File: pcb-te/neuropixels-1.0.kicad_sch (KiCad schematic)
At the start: 15 parts, among them J2 1-2013496-8, U6 MAX40111ANT

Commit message: Added new fields (OEPS PN, MPN, and Type) to all components.
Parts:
- C28, C29: MPN (none) -> GRM033R61E104KE14J; OEPS PN (none) -> OEPS010035; Type (none) -> SMD
- C30: MPN (none) -> GRM033R71E103KE14D; OEPS PN (none) -> OEPS010037; Type (none) -> SMD
- C31: MPN (none) -> GRM0335C1H270GA01D; OEPS PN (none) -> OEPS010029; Type (none) -> SMD
- J2: MPN (none) -> 1-2013496-8; OEPS PN (none) -> OEPS070051; Type (none) -> SMD
- R? (x3): MPN (none) -> RC0201FR-071KL; OEPS PN (none) -> OEPS020065; Type (none) -> SMD
- R?: MPN (none) -> RMCF0201FT22R0CT-ND; OEPS PN (none) -> OEPS020069; Type (none) -> SMD
- R?: MPN (none) -> CRCW02017K15FKED; OEPS PN (none) -> OEPS020058; Type (none) -> SMD
- R?: MPN (none) -> CRCW020110K0FNED; OEPS PN (none) -> OEPS020066; Type (none) -> SMD
- R?: MPN (none) -> RC0201FR-0749R9L; OEPS PN (none) -> OEPS020068; Type (none) -> SMD
- U6: MPN (none) -> MAX40111ANT+; OEPS PN (none) -> OEPS080048; Type (none) -> SMD
- U?: MPN (none) -> DSC6101MA3B-PROGT; OEPS PN (none) -> OEPS080049; Type (none) -> SMD
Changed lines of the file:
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@@
+      (effects (font (size 1.27 1.27)) hide)
+    )
+    (property "MPN" "GRM033R61E104KE14J" (at 59.69 72.39 0)
+      (effects (font (size 1.27 1.27)) hide)
+    )
+    (property "OEPS PN" "OEPS010035" (at 59.69 72.39 0)
+      (effects (font (size 1.27 1.27)) hide)
+    )
+    (property "Type" "SMD" (at 59.69 72.39 0)
+      (effects (font (size 1.27 1.27)) hide)
+    )
+    (property "test" "" (at 59.69 72.39 0)
       (effects (font (size 1.27 1.27)) hide)
     )
@@
     )
     (property "Datasheet" "https://www.analog.com/media/en/technical-documentation/data-sheets/MAX40110-MAX40111.pdf" (at 82.55 66.04 0)
+      (effects (font (size 1.27 1.27)) hide)
+    )
+    (property "MPN" "MAX40111ANT+" (at 81.28 69.85 0)
+      (effects (font (size 1.27 1.27)) hide)
+    )
+    (property "OEPS PN" "OEPS080048" (at 81.28 69.85 0)
+      (effects (font (size 1.27 1.27)) hide)
+    )
+    (property "Type" "SMD" (at 81.28 69.85 0)
+      (effects (font (size 1.27 1.27)) hide)
+    )
+    (property "test" "" (at 81.28 69.85 0)
       (effects (font (size 1.27 1.27)) hide)
     )
@@
       (effects (font (size 1.27 1.27)) hide)
     )
+    (property "MPN" "RC0201FR-071KL" (at 59.69 62.23 0)
+      (effects (font (size 1.27 1.27)) hide)
+    )
+    (property "OEPS PN" "OEPS020065" (at 59.69 62.23 0)
+      (effects (font (size 1.27 1.27)) hide)
+    )
+    (property "Type" "SMD" (at 59.69 62.23 0)
+      (effects (font (size 1.27 1.27)) hide)
+    )
+    (property "test" "" (at 59.69 62.23 0)
+      (effects (font (size 1.27 1.27)) hide)
+    )
     (pin "1")
     (pin "2")
@@
       (effects (font (size 1.27 1.27)) hide)
     )
+    (property "MPN" "RMCF0201FT22R0CT-ND" (at 107.95 130.81 0)
+      (effects (font (size 1.27 1.27)) hide)
+    )
+    (property "OEPS PN" "OEPS020069" (at 107.95 130.81 0)
+      (effects (font (size 1.27 1.27)) hide)
+    )
+    (property "Type" "SMD" (at 107.95 130.81 0)
+      (effects (font (size 1.27 1.27)) hide)
+    )
+    (property "test" "" (at 107.95 130.81 0)
+      (effects (font (size 1.27 1.27)) hide)
+    )
     (pin "1")
     (pin "2")
@@
     )
     (property "Datasheet" "https://ww1.microchip.com/downloads/en/DeviceDoc/DSC61xxB-Ultra-Small-Ultra-Low-Power-MEMS-Oscillator-DS20006155A.pdf" (at 77.47 135.89 0)
+      (effects (font (size 1.27 1.27)) hide)
+    )
+    (property "MPN" "DSC6101MA3B-PROGT" (at 77.47 133.35 0)
+      (effects (font (size 1.27 1.27)) hide)
+    )
+    (property "OEPS PN" "OEPS080049" (at 77.47 133.35 0)
+      (effects (font (size 1.27 1.27)) hide)
+    )
+    (property "Type" "SMD" (at 77.47 133.35 0)
+      (effects (font (size 1.27 1.27)) hide)
+    )
+    (property "test" "" (at 77.47 133.35 0)
       (effects (font (size 1.27 1.27)) hide)
     )
@@
       (effects (font (size 1.27 1.27)) hide)
     )
+    (property "MPN" "GRM0335C1H270GA01D" (at 115.57 135.89 0)
+      (effects (font (size 1.27 1.27)) hide)
+    )
+    (property "OEPS PN" "OEPS010029" (at 115.57 135.89 0)
+      (effects (font (size 1.27 1.27)) hide)
+    )
+    (property "Type" "SMD" (at 115.57 135.89 0)
+      (effects (font (size 1.27 1.27)) hide)
+    )
+    (property "test" "" (at 115.57 135.89 0)
+      (effects (font (size 1.27 1.27)) hide)
+    )
     (pin "1")
     (pin "2")
@@
       (effects (font (size 1.27 1.27)) hide)
     )
+    (property "MPN" "GRM033R71E103KE14D" (at 53.34 135.89 0)
+      (effects (font (size 1.27 1.27)) hide)
+    )
+    (property "OEPS PN" "OEPS010037" (at 53.34 135.89 0)
+      (effects (font (size 1.27 1.27)) hide)
+    )
+    (property "Type" "SMD" (at 53.34 135.89 0)
+      (effects (font (size 1.27 1.27)) hide)
+    )
+    (property "test" "" (at 53.34 135.89 0)
+      (effects (font (size 1.27 1.27)) hide)
+    )
     (pin "1")
     (pin "2")
@@
     )
     (property "Tolerance" "1%" (at 95.25 88.9 0)
+      (effects (font (size 1.27 1.27)) hide)
+    )
+    (property "MPN" "CRCW02017K15FKED" (at 95.25 88.9 0)
+      (effects (font (size 1.27 1.27)) hide)
+    )
+    (property "OEPS PN" "OEPS020058" (at 95.25 88.9 0)
+      (effects (font (size 1.27 1.27)) hide)
+    )
+    (property "Type" "SMD" (at 95.25 88.9 0)
+      (effects (font (size 1.27 1.27)) hide)
+    )
+    (property "test" "" (at 95.25 88.9 0)
       (effects (font (size 1.27 1.27)) hide)
     )
@@
       (effects (font (size 1.27 1.27)) hide)
     )
+    (property "MPN" "" (at 115.57 121.92 0)
+      (effects (font (size 1.27 1.27)) hide)
+    )
+    (property "OEPS PN" "" (at 115.57 121.92 0)
+      (effects (font (size 1.27 1.27)) hide)
+    )
+    (property "Type" "" (at 115.57 121.92 0)
+      (effects (font (size 1.27 1.27)) hide)
+    )
+    (property "test" "" (at 115.57 121.92 0)
+      (effects (font (size 1.27 1.27)) hide)
+    )
     (pin "1")
     (pin "2")
@@
       (effects (font (size 1.27 1.27)) hide)
     )
+    (property "MPN" "CRCW020110K0FNED" (at 119.38 69.85 0)
+      (effects (font (size 1.27 1.27)) hide)
+    )
+    (property "OEPS PN" "OEPS020066" (at 119.38 69.85 0)
+      (effects (font (size 1.27 1.27)) hide)
+    )
+    (property "Type" "SMD" (at 119.38 69.85 0)
+      (effects (font (size 1.27 1.27)) hide)
+    )
+    (property "test" "" (at 119.38 69.85 0)
+      (effects (font (size 1.27 1.27)) hide)
+    )
     (pin "1")
     (pin "2")
@@
     )
     (property "Datasheet" "https://www.mouser.com/datasheet/2/418/8/TYELS72827_1-2524186.pdf" (at 182.88 115.57 0)
+      (effects (font (size 1.27 1.27)) hide)
+    )
+    (property "MPN" "1-2013496-8" (at 182.88 115.57 0)
+      (effects (font (size 1.27 1.27)) hide)
+    )
+    (property "OEPS PN" "OEPS070051" (at 182.88 115.57 0)
+      (effects (font (size 1.27 1.27)) hide)
+    )
+    (property "Type" "SMD" (at 182.88 115.57 0)
+      (effects (font (size 1.27 1.27)) hide)
+    )
+    (property "test" "" (at 182.88 115.57 0)
       (effects (font (size 1.27 1.27)) hide)
     )
@@
       (effects (font (size 1.27 1.27)) hide)
     )
+    (property "MPN" "RC0201FR-071KL" (at 95.25 54.61 0)
+      (effects (font (size 1.27 1.27)) hide)
+    )
+    (property "OEPS PN" "OEPS020065" (at 95.25 54.61 0)
+      (effects (font (size 1.27 1.27)) hide)
+    )
+    (property "Type" "SMD" (at 95.25 54.61 0)
+      (effects (font (size 1.27 1.27)) hide)
+    )
+    (property "test" "" (at 95.25 54.61 0)
+      (effects (font (size 1.27 1.27)) hide)
+    )
     (pin "1")
     (pin "2")
@@
       (effects (font (size 1.27 1.27)) hide)
     )
+    (property "MPN" "RC0201FR-071KL" (at 59.69 54.61 0)
+      (effects (font (size 1.27 1.27)) hide)
+    )
+    (property "OEPS PN" "OEPS020065" (at 59.69 54.61 0)
+      (effects (font (size 1.27 1.27)) hide)
+    )
+    (property "Type" "SMD" (at 59.69 54.61 0)
+      (effects (font (size 1.27 1.27)) hide)
+    )
+    (property "test" "" (at 59.69 54.61 0)
+      (effects (font (size 1.27 1.27)) hide)
+    )
     (pin "1")
     (pin "2")
@@
       (effects (font (size 1.27 1.27)) hide)
     )
+    (property "MPN" "RC0201FR-0749R9L" (at 130.81 76.2 0)
+      (effects (font (size 1.27 1.27)) hide)
+    )
+    (property "OEPS PN" "OEPS020068" (at 130.81 76.2 0)
+      (effects (font (size 1.27 1.27)) hide)
+    )
+    (property "Type" "SMD" (at 130.81 76.2 0)
+      (effects (font (size 1.27 1.27)) hide)
+    )
+    (property "test" "" (at 130.81 76.2 0)
+      (effects (font (size 1.27 1.27)) hide)
+    )
     (pin "1")
     (pin "2")
@@
       (effects (font (size 1.27 1.27)) hide)
     )
+    (property "MPN" "GRM033R61E104KE14J" (at 67.31 39.37 0)
+      (effects (font (size 1.27 1.27)) hide)
+    )
+    (property "OEPS PN" "OEPS010035" (at 67.31 39.37 0)
+      (effects (font (size 1.27 1.27)) hide)
+    )
+    (property "Type" "SMD" (at 67.31 39.37 0)
+      (effects (font (size 1.27 1.27)) hide)
+    )
+    (property "test" "" (at 67.31 39.37 0)
+      (effects (font (size 1.27 1.27)) hide)
+    )

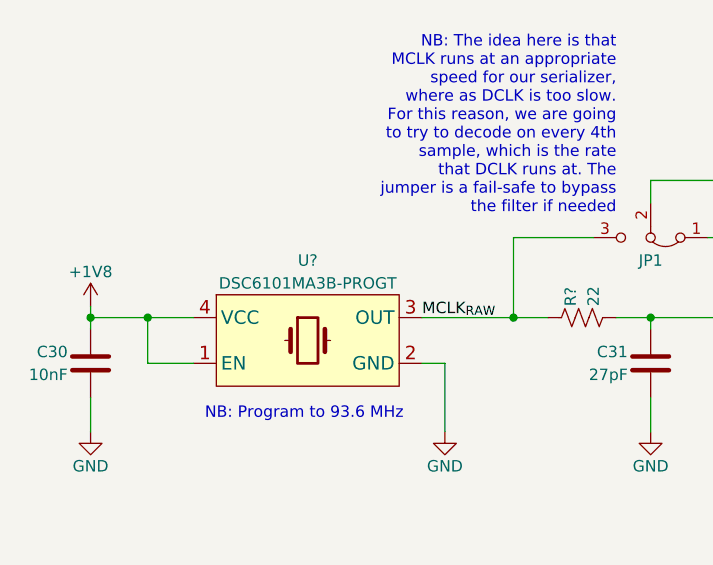
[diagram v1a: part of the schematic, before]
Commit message: Update oscillator part number to high-drive variant
- Orignal part number was too weak to reliably drive clock line on flex
  connector
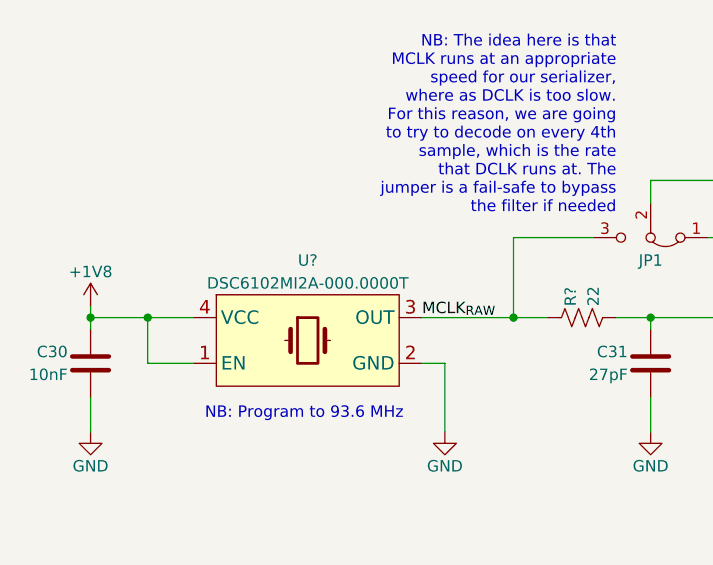
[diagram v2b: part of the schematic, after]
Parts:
- U?: value DSC6101MA3B-PROGT -> DSC6102MI2A-000.0000T; OEPS PN OEPS080049 -> OEPS080092
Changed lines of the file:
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@@
       (effects (font (size 1.27 1.27)))
     )
-    (property "Value" "DSC6101MA3B-PROGT" (at 77.47 127 0)
+    (property "Value" "DSC6102MI2A-000.0000T" (at 77.47 127 0)
       (effects (font (size 1.27 1.27)))
     )
@@
       (effects (font (size 1.27 1.27)) hide)
     )
-    (property "OEPS PN" "OEPS080049" (at 77.47 133.35 0)
+    (property "OEPS PN" "OEPS080092" (at 77.47 133.35 0)
       (effects (font (size 1.27 1.27)) hide)
     )
